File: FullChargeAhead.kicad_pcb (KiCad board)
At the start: 2 copper layers, 19 parts, among them CON101 USB-MICRO-B, P101 CONN_01X02, P102 JST 2 Pin, U101 MCP73834-FCI/UN

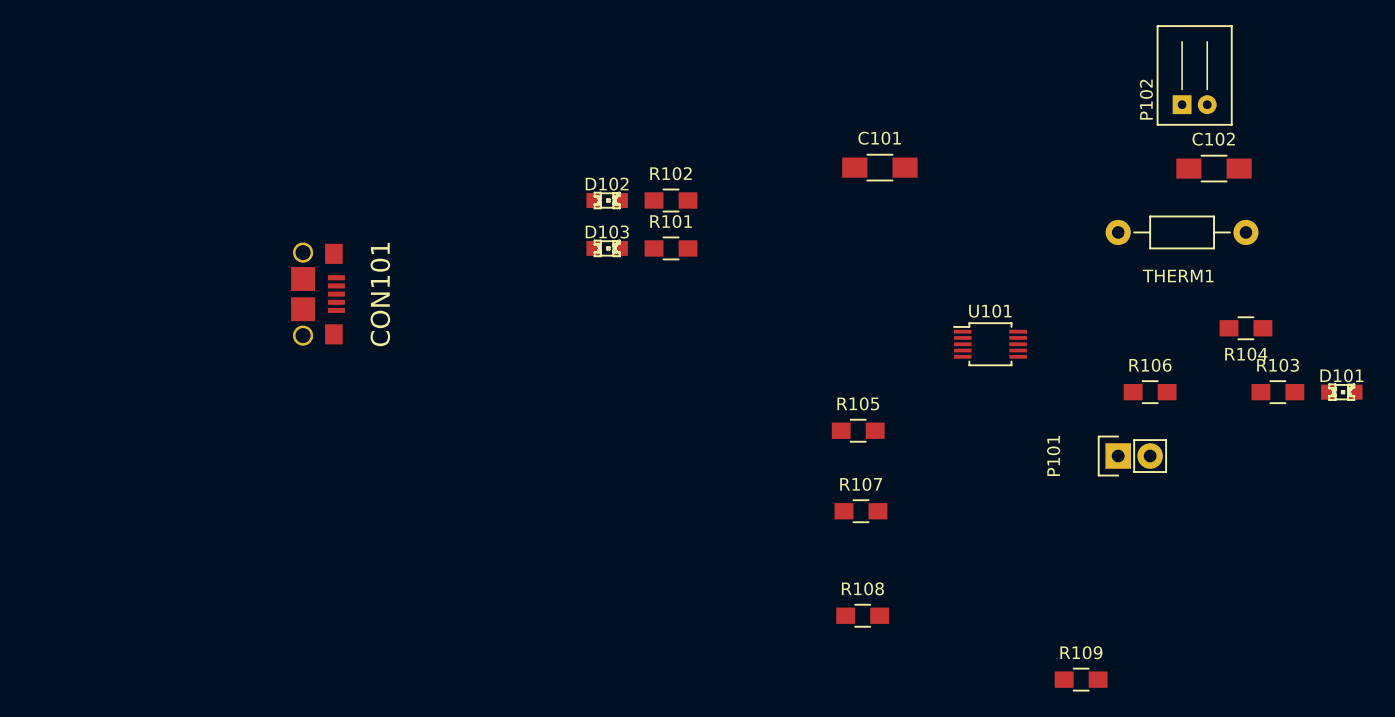
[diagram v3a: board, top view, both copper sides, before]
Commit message: Front Cu Layout done
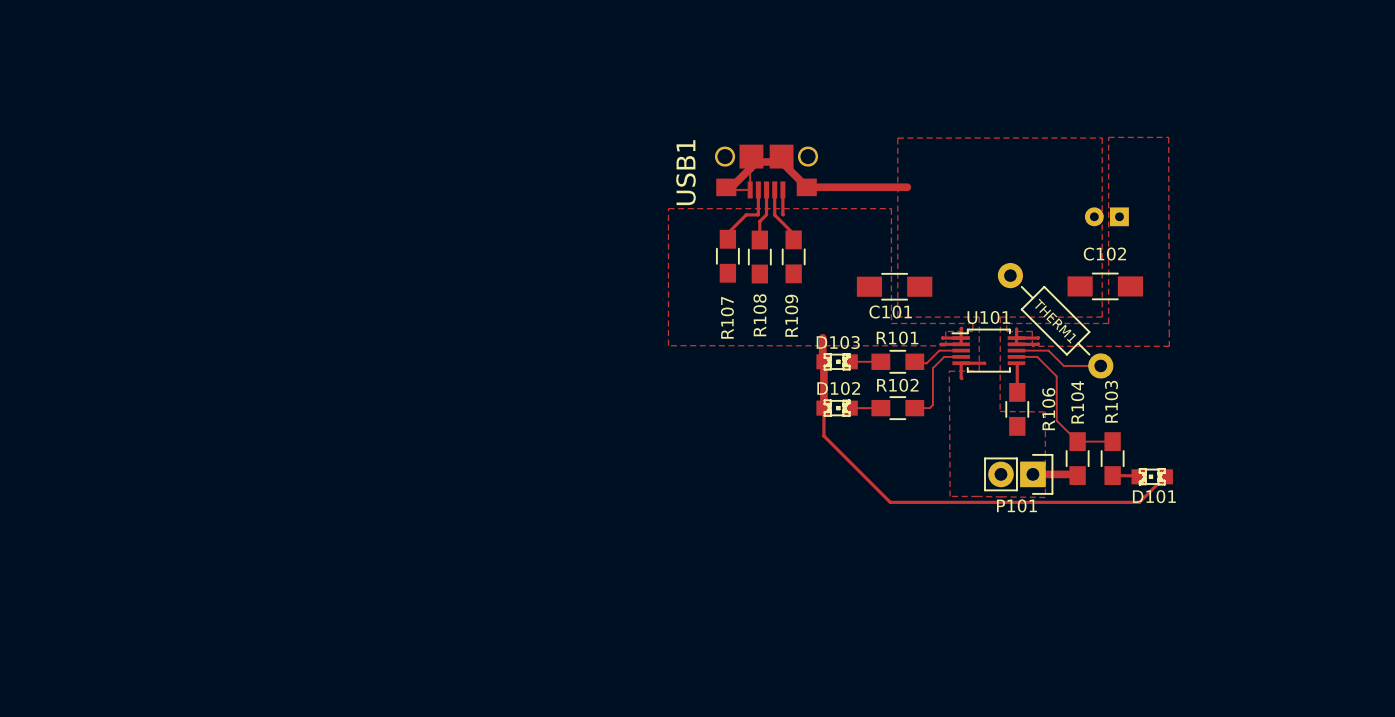
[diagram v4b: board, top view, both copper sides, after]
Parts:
- removed CON101: USB-MICRO-B, fca-lib:USB_Micro_B
- removed R105: 10K, Resistors_SMD:R_0805_HandSoldering
- added USB1: USB-MICRO-B, fca-lib:USB_Micro_B, F.Cu at (142.2, 65.1)
- P102: moved to B.Cu
- moved R109 40.7 mm to (144.4, 73.1), turned to 270 degrees
- moved R108 29.7 mm to (141.7, 73.1), turned to 270 degrees
- moved D102 24.6 mm to (147.8, 85.1)
- moved R102 24.5 mm to (152.7, 85.1), turned to 180 degrees
- moved R107 22.9 mm to (139.1, 73.0), turned to 270 degrees
- moved D103 20.4 mm to (147.8, 81.4)
- moved R101 20.2 mm to (152.7, 81.4)
- moved R104 16.9 mm to (167.0, 89.1), turned to 90 degrees
- moved D101 16.5 mm to (172.9, 90.6), turned to 180 degrees
- moved R103 14.2 mm to (169.7, 89.1), turned to 90 degrees
- moved C102 12.8 mm to (169.2, 75.4), turned to 180 degrees
- moved THERM1 12.3 mm to (165.2, 78.1), turned to 315 degrees
- moved R106 10.7 mm to (162.2, 85.2), turned to 90 degrees
- moved P102 10.2 mm to (170.3, 69.9)
- moved C101 9.55 mm to (152.4, 75.4)
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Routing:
- net /Vdd: track 0.00 -> 44.4 mm
- net GND: track 0.00 -> 23.4 mm
- net Net-(R103-Pad2): track 0.00 -> 12.5 mm
- net Net-(R102-Pad1): track 0.00 -> 7.26 mm
- net Net-(THERM1-Pad2): track 0.00 -> 7.20 mm
- net Net-(R107-Pad1): track 0.00 -> 5.48 mm
- net /Vbat: track 0.00 -> 4.76 mm
- net Net-(R109-Pad1): track 0.00 -> 4.60 mm
- net Net-(P101-Pad1): track 0.00 -> 4.29 mm
- net Net-(R108-Pad1): track 0.00 -> 4.21 mm
- net Net-(R101-Pad2): track 0.00 -> 4.12 mm
- net Net-(D103-Pad2): track 0.00 -> 2.43 mm
- net Net-(D102-Pad2): track 0.00 -> 2.43 mm
- net Net-(R106-Pad2): track 0.00 -> 2.35 mm
- net Net-(D101-Pad2): track 0.00 -> 2.13 mm
- added copper zone on F.Cu, net /Vbat
- added copper zone on F.Cu, net /Vdd
- added copper zone on F.Cu, net GND
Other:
- net class Default: clearance 0.254 -> 0.1524; trace_width 0.254 -> 0.1524; via_dia 0.889 -> 0.6858; via_drill 0.635 -> 0.3302
- rule trace_clearance: 0.254 -> 0.1524
- rule trace_min: 0.254 -> 0.1524
- rule via_min_drill: 0.508 -> 0.3302
- rule via_min_size: 0.889 -> 0.6858

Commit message: Back Cu Layout and changes to front Cu. Also edge cuts added
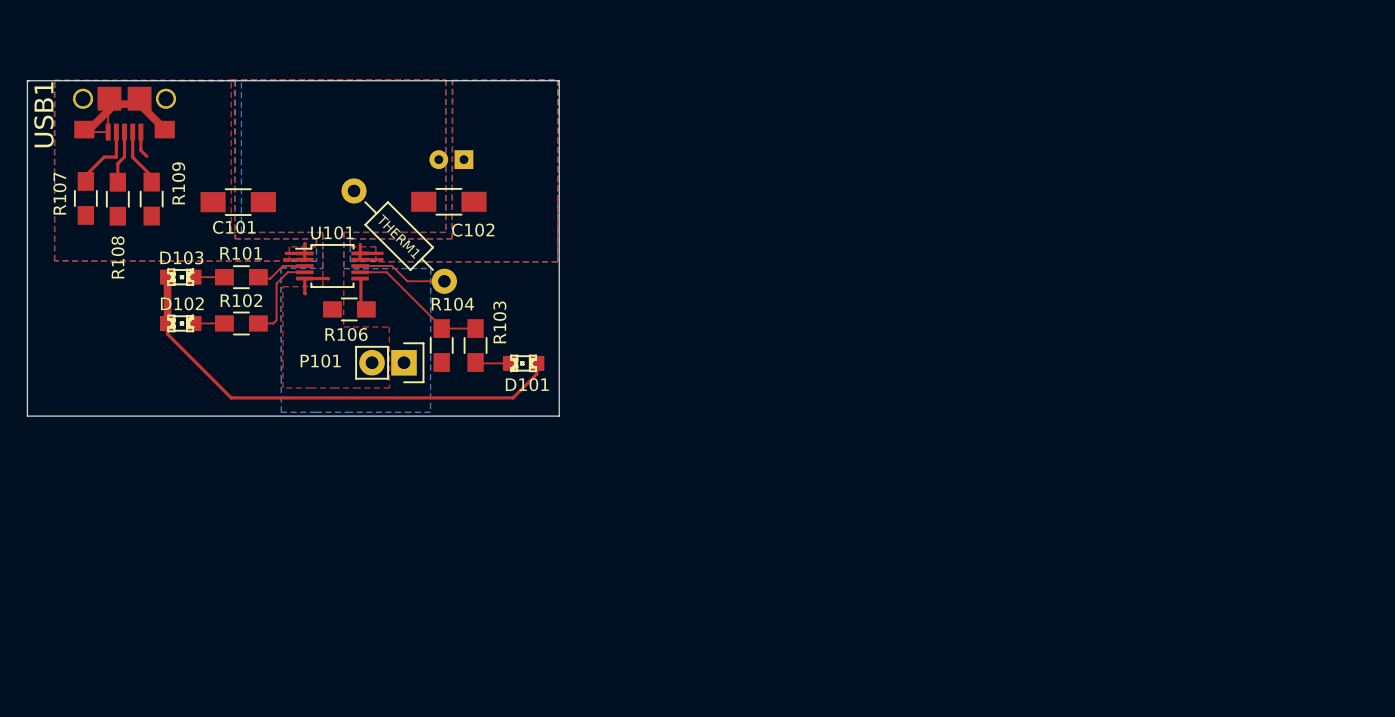
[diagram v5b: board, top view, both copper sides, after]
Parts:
- moved R106 53.7 mm to (109.0, 77.2), turned to 0 degrees
- moved THERM1 52.6 mm to (113.0, 71.4)
- moved C101 52.6 mm to (100.2, 68.7)
- moved D102 52.6 mm to (95.6, 78.4)
- moved D103 52.6 mm to (95.6, 74.7)
- moved R101 52.6 mm to (100.5, 74.7)
- moved R102 52.6 mm to (100.5, 78.4)
- moved U101 52.6 mm to (107.7, 73.8)
- moved C102 52.6 mm to (117.0, 68.7)
- moved P102 52.3 mm to (118.2, 65.3)
- moved R103 51.5 mm to (119.1, 80.1)
- moved R104 51.4 mm to (116.4, 80.1)
- moved R109 51.3 mm to (93.3, 68.5)
- moved R107 51.3 mm to (88.1, 68.4)
- moved R108 51.3 mm to (90.6, 68.5)
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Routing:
- net GND: track 23.4 -> 15.4 mm
- net Net-(P101-Pad1): track 4.29 -> 0.00 mm
- net Net-(R103-Pad2): track 12.5 -> 11.1 mm
- net Net-(D101-Pad2): track 2.13 -> 2.80 mm
- added copper zone on B.Cu, net /Vbat
- added copper zone on B.Cu, net /Vdd
- added copper zone on B.Cu, net GND
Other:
- board outline added: 42.3 x 26.7 mm

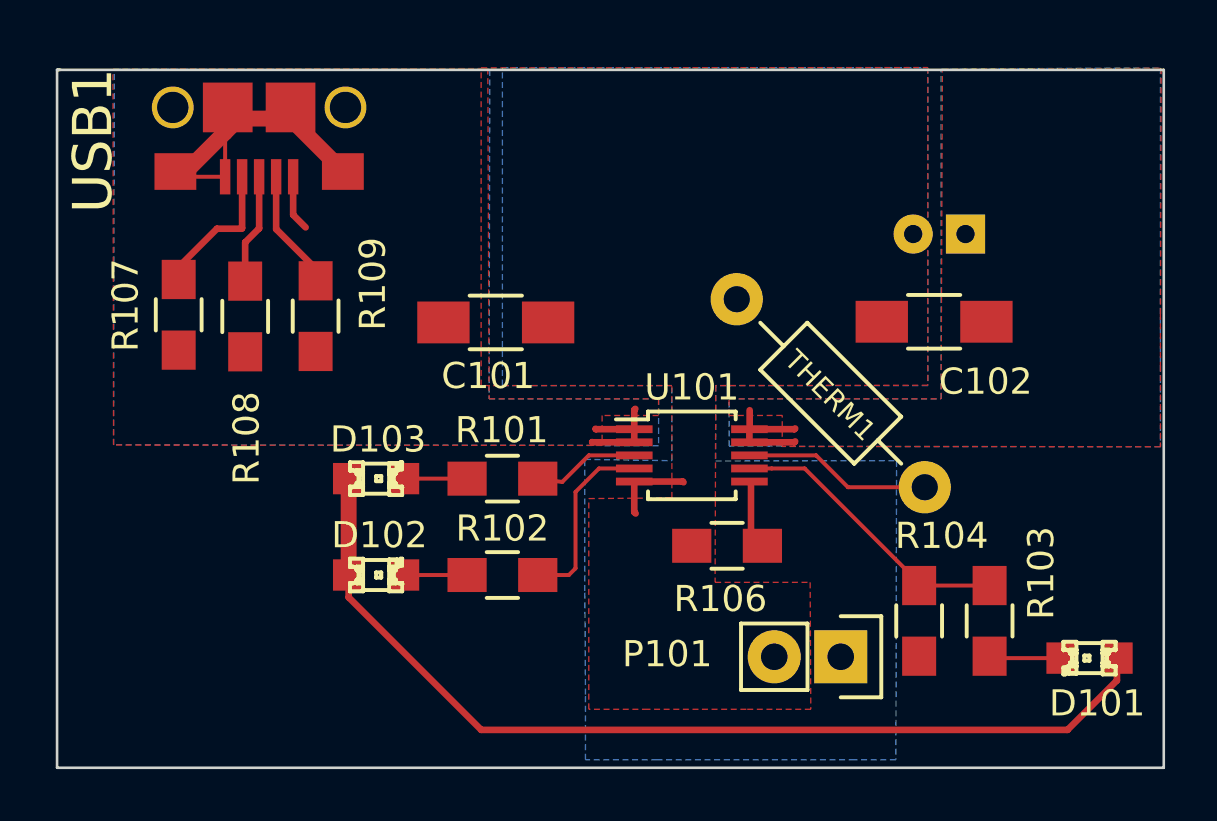
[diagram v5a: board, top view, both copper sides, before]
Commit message: Back Cu Layout and changes to front Cu. Also edge cuts added #2
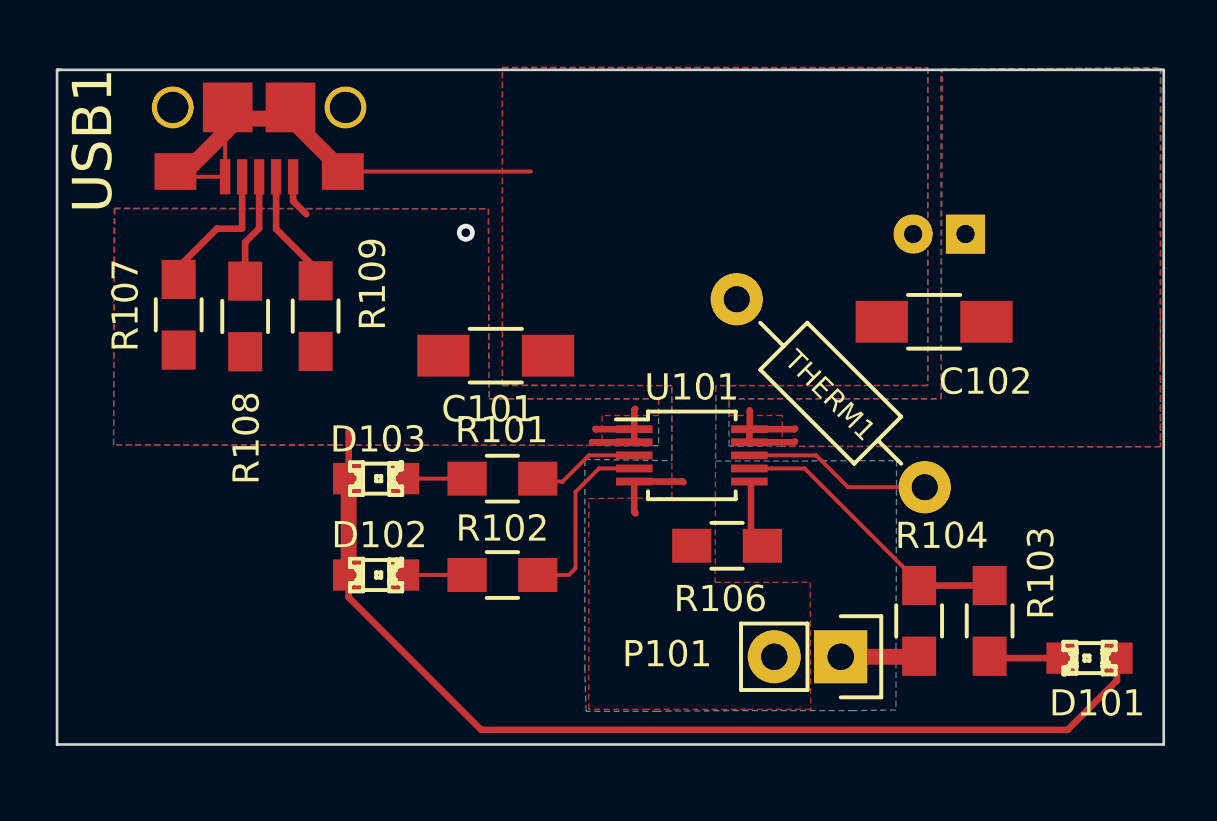
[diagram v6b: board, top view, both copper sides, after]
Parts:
- moved C101 1.27 mm to (100.2, 70.0)
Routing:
- net GND: track 15.4 -> 22.6 mm
- net Net-(P101-Pad1): track 0.00 -> 3.01 mm
- net /Vdd: track 44.3 -> 45.7 mm
- net (no net): vias 0 -> 1
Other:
- board size 42.3 x 26.7 mm -> 42.3 x 25.8 mm

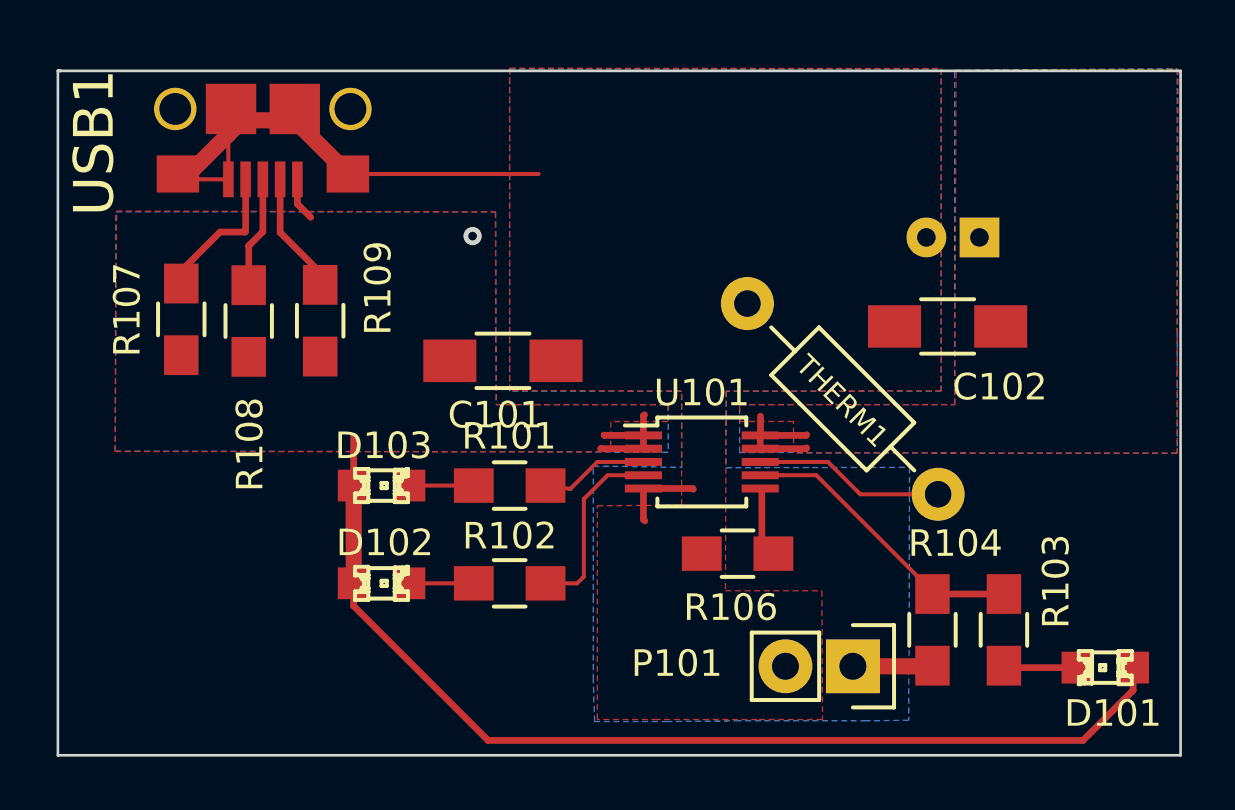
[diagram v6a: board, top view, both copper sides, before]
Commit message: Base vias for stitching added
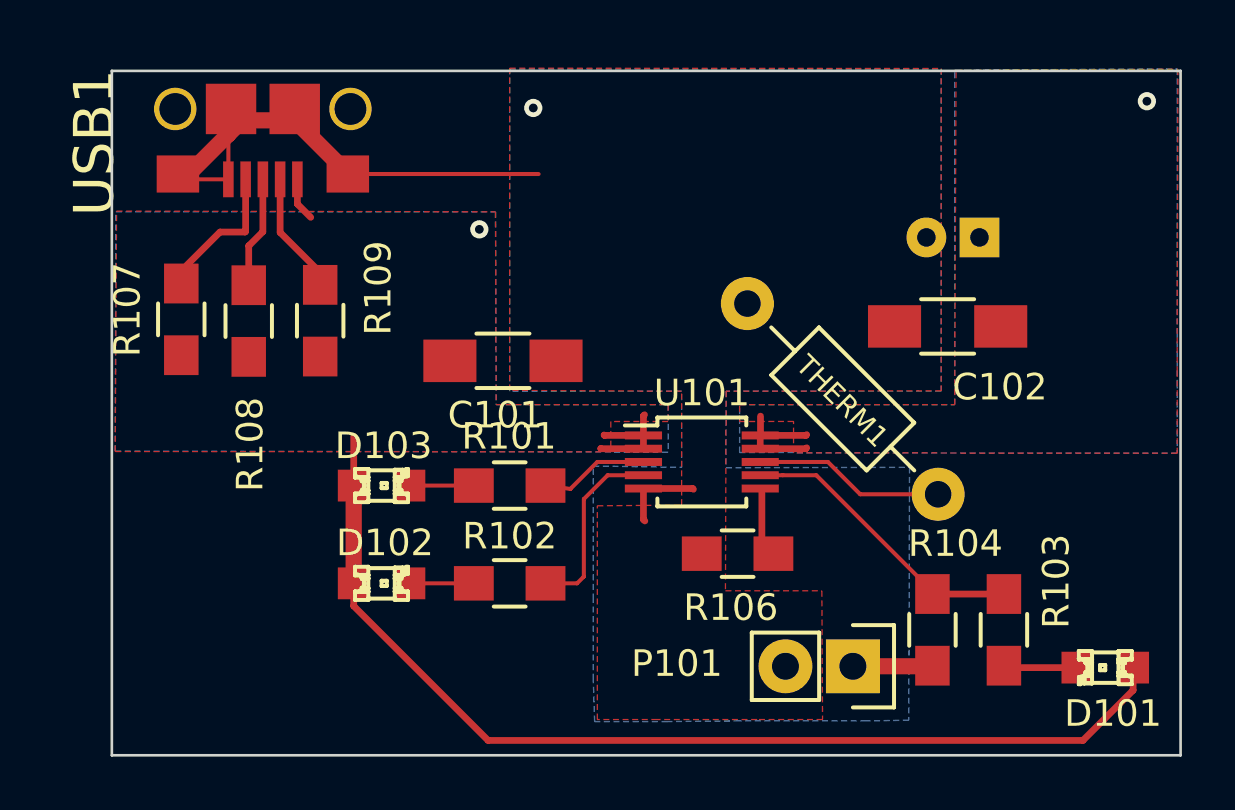
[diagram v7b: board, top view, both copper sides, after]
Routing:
- net GND: vias 0 -> 1
- net /Vdd: vias 0 -> 1
- net /Vbat: vias 0 -> 1
- net (no net): vias 1 -> 0
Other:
- board size 42.3 x 25.8 mm -> 40.3 x 25.8 mm

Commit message: Via stitched
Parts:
- moved R107 1.27 mm to (89.4, 68.4)
- moved R109 1.27 mm to (94.6, 68.5)
- moved R108 1.27 mm to (91.9, 68.5)
- moved USB1 1.27 mm to (92.4, 60.5)
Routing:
- net GND: track 22.6 -> 129.9 mm, vias 1 -> 44
- net /Vbat: track 4.76 -> 59.2 mm, vias 1 -> 25
- net /Vdd: track 45.7 -> 90.1 mm, vias 1 -> 24
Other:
- board size 40.3 x 25.8 mm -> 38.6 x 25.8 mm
